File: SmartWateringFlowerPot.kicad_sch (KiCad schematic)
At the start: 0 parts

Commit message: Add first schematic draft
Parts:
- added C1: 10uF input, Capacitor_SMD:C_0805_2012Metric, symbol Device:C
- added C2: 22uF output, Capacitor_SMD:C_0805_2012Metric, symbol Device:C
- added C3: 100nF BST, Capacitor_SMD:C_0805_2012Metric, symbol Device:C
- added D1: SS34 flyback, Diode_SMD:D_SMA, symbol Device:D_Schottky
- added J1: USB-C 5V + USB2, symbol Connector:USB_C_Receptacle_USB2.0_14P
- added J2: PUMP 5V, Connector_JST:JST_XH_B2B-XH-A_1x02_P2.50mm_Vertical, symbol Connector_Generic:Conn_01x02
- added J3: MOISTURE, Connector_JST:JST_XH_B3B-XH-A_1x03_P2.50mm_Vertical, symbol Connector_Generic:Conn_01x03
- added J4: RESERVOIR_SW, Connector_JST:JST_XH_B2B-XH-A_1x02_P2.50mm_Vertical, symbol Connector_Generic:Conn_01x02
- added J5: FLOW optional, Connector_JST:JST_XH_B3B-XH-A_1x03_P2.50mm_Vertical, symbol Connector_Generic:Conn_01x03
- added J6: UI OLED/ENC/LED, Connector_JST:JST_XH_B9B-XH-A_1x09_P2.50mm_Vertical, symbol Connector_Generic:Conn_01x09
- added J7: DEBUG 3V3/GND/TX/RX/EN/BOOT, Connector_PinHeader_2.54mm:PinHeader_1x06_P2.54mm_Vertical, symbol Connector_Generic:Conn_01x06
- added L1: 2.2uH TBD, symbol Device:L
- added Q1: AO3400A, Package_TO_SOT_SMD:SOT-23, symbol Transistor_FET:Q_NMOS_GSD
- added R1: 5.1k CC1, Resistor_SMD:R_0805_2012Metric, symbol Device:R
- added R2: 5.1k CC2, Resistor_SMD:R_0805_2012Metric, symbol Device:R
- added R3: 10k EN pullup, Resistor_SMD:R_0805_2012Metric, symbol Device:R
- added R4: 220R gate, Resistor_SMD:R_0805_2012Metric, symbol Device:R
- added R5: 100k pulldown, Resistor_SMD:R_0805_2012Metric, symbol Device:R
- added R6: 4.7k SDA, Resistor_SMD:R_0805_2012Metric, symbol Device:R
- added R7: 4.7k SCL, Resistor_SMD:R_0805_2012Metric, symbol Device:R
- added R8: 10k reservoir pullup, Resistor_SMD:R_0805_2012Metric, symbol Device:R
- added U1: ESP32-S3-WROOM-1-N8, RF_Module:ESP32-S3-WROOM-1, symbol RF_Module:ESP32-S3-WROOM-1
- added U2: AP63203WU-7, Package_TO_SOT_SMD:TSOT-23-6, symbol Regulator_Switching:AP63200WU
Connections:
- new net: Q1.1 (G), R4.2, R5.1
- new net: D1.2 (A), J2.2 (Pin_2), Q1.3 (D)
- new net: J1.A5 (CC1), R1.1
- new net: J1.A6 (D+), J1.B6 (D+), U1.14 (USB_D+)
- new net: J1.A7 (D-), J1.B7 (D-), U1.13 (USB_D-)
- new net: J1.B5 (CC2), R2.1
- new net: R4.1, U1.4 (IO4)
- new net: J4.1 (Pin_1), R8.1, U1.21 (IO13)
- new net: C3.1, U2.6 (BST)
- new net: C3.2, L1.2, U2.5 (SW)
- new net: J6.4 (Pin_4), J6.7 (Pin_7), J7.4 (Pin_4), R7.2, U1.17 (IO9), U1.20 (IO12), U1.36 (RXD0)
- new net: J3.3 (Pin_3), U1.39 (IO1)
- new net: J5.3 (Pin_3), U1.22 (IO14)
- new net: J7.3 (Pin_3), J7.5 (Pin_5), R3.1, U1.3 (EN), U1.37 (TXD0)
- new net: J6.3 (Pin_3), J6.5 (Pin_5), J6.6 (Pin_6), J6.8 (Pin_8), J6.9 (Pin_9), R6.2, U1.12 (IO8), U1.18 (IO10), U1.19 (IO11), U1.8 (IO15), U1.9 (IO16)
- new net: J7.6 (Pin_6), U1.27 (IO0)
- new net +3V3: C2.1, J3.1 (Pin_1), J5.1 (Pin_1), J6.1 (Pin_1), J7.1 (Pin_1), L1.1, R3.2, R6.1, R7.1, R8.2, U1.2 (3V3), U2.1 (FB)
- new net +5V: C1.1, D1.1 (K), J1.A4 (VBUS), J1.A9 (VBUS), J1.B4 (VBUS), J1.B9 (VBUS), J2.1 (Pin_1), U2.2 (EN), U2.3 (IN)
- new net GND: C1.2, C2.2, J1.A1 (GND), J1.A12 (GND), J1.B1 (GND), J1.B12 (GND), J1.S1 (SHIELD), J3.2 (Pin_2), J4.2 (Pin_2), J5.2 (Pin_2), J6.2 (Pin_2), J7.2 (Pin_2), Q1.2 (S), R1.2, R2.2, R5.2, U1.1 (GND), U1.40 (GND), U1.41 (GND), U2.4 (GND)
- no-connect marks 0 -> 20
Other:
- note added: "3.3V buck regulator"
- note added: "AO3400A low-side driver: gate resistor, 100k pulldown, SS34 flyback diode."
- note added: "ESP32-S3 + connectors"
- note added: "FLOW_PULSE must be level shifted if selected sensor outputs 5V pulses."
- note added: "Follow AP63203 datasheet layout exactly: compact input cap, inductor, BST loop, and FB node."
- note added: "J6: 3V3, GND, SDA, SCL, ENC_A, ENC_B, ENC_SW, ERROR_LED, STATUS_LED."
- note added: "J7 pinout: 3V3, GND, TXD0, RXD0, EN, IO0/BOOT."
- note added: "MOISTURE_ADC uses IO1 / ADC1-capable pin. Sensor output must be <= 3.3V."
- note added: "Pump low-side driver"
- note added: "Reservoir switch default: pullup to 3V3, switch closes to GND."
- note added: "Smart Pot V2 Rev A - first schematic draft"
- note added: "USB D-/D+ routed to ESP32-S3 native USB pins."
- note added: "USB-C input + native USB"
- note added: "Verify exact footprints, connector pin order, ESP32 boot pins, and AP63203 layout before PCB routing."

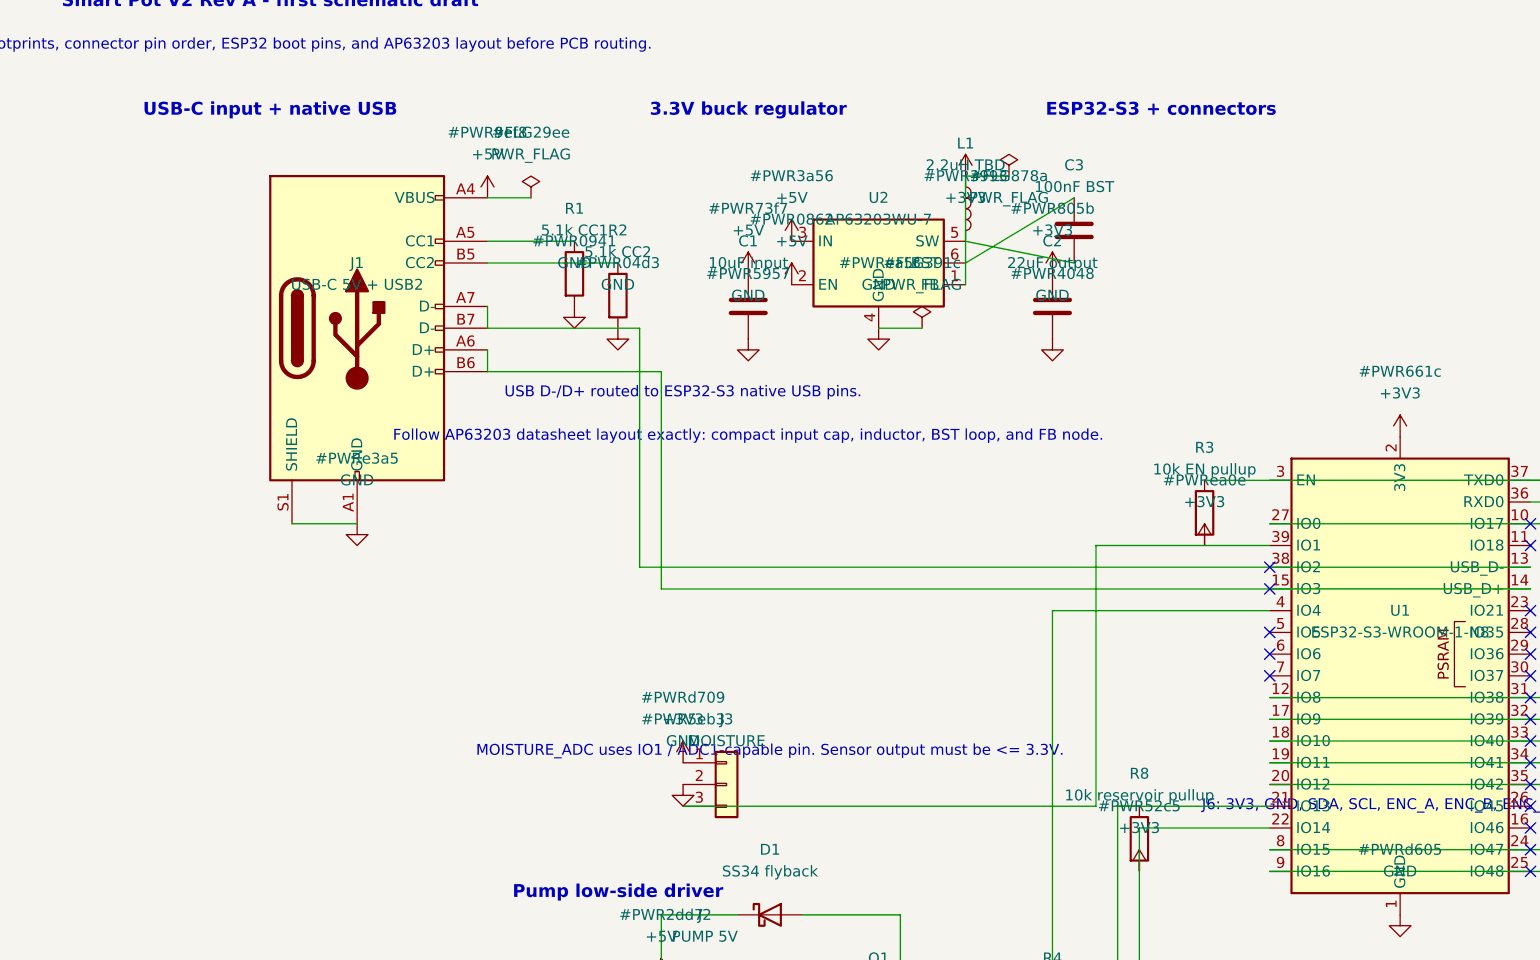
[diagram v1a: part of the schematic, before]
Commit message: Prepare schematic for PCB pass two
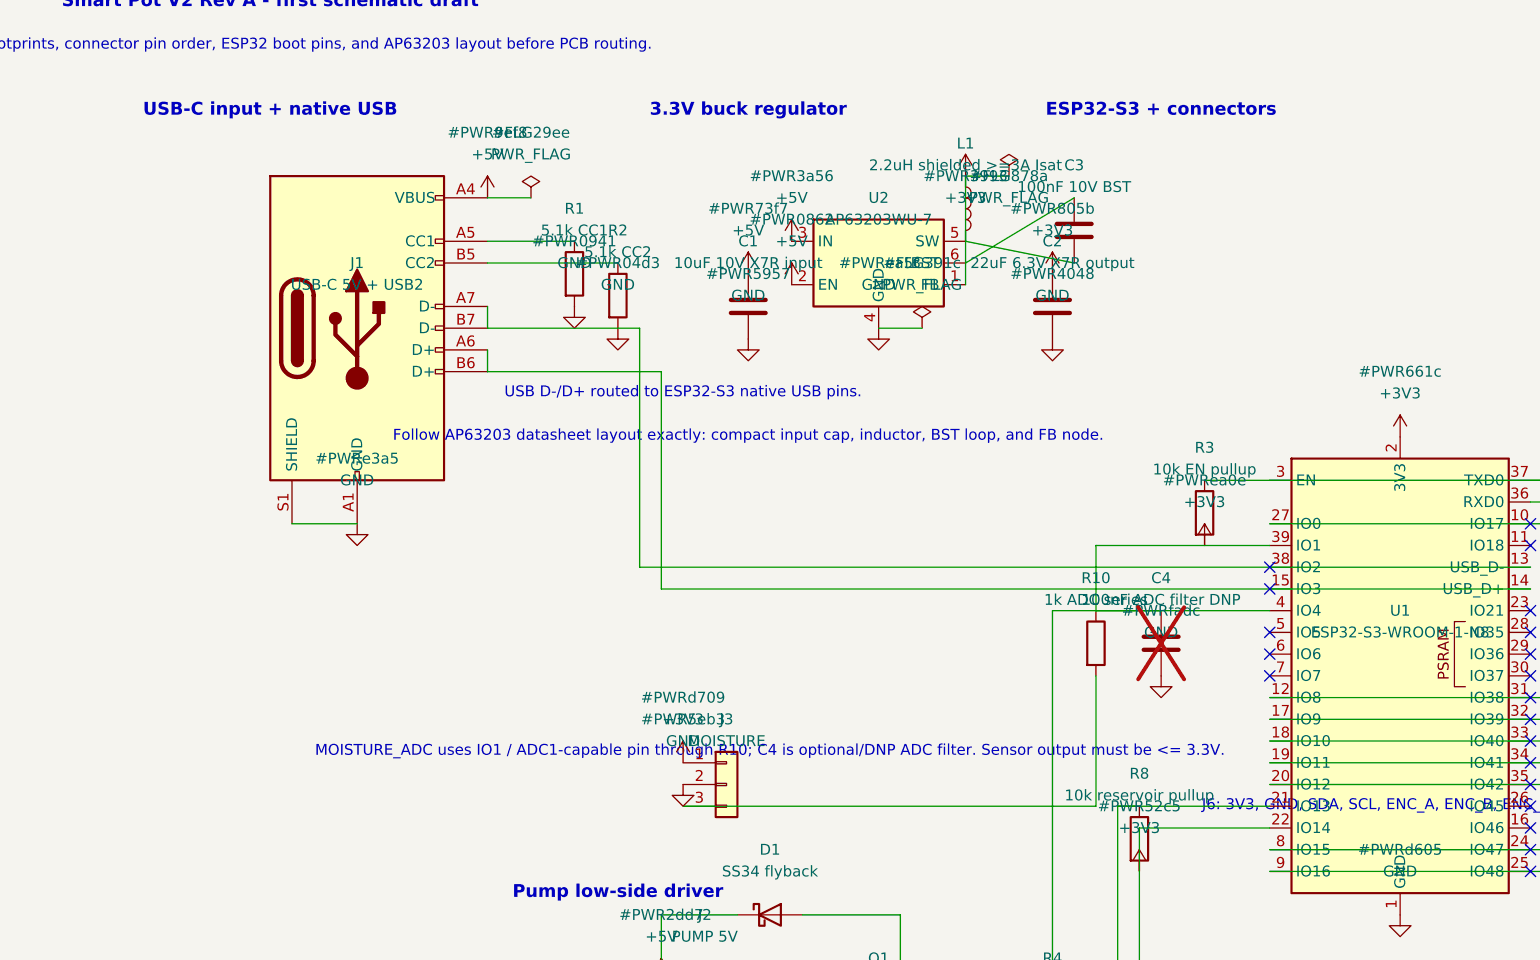
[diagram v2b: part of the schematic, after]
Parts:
- added C4: 100nF ADC filter DNP, Capacitor_SMD:C_0805_2012Metric, symbol Device:C
- added R10: 1k ADC series, Resistor_SMD:R_0805_2012Metric, symbol Device:R
- C1: value 10uF input -> 10uF 10V X7R input
- C2: value 22uF output -> 22uF 6.3V X7R output
- C3: value 100nF BST -> 100nF 10V BST
- J1: footprint (none) -> Connector_USB:USB_C_Receptacle_GCT_USB4105-xx-A_16P_TopMnt_Horizontal
- L1: value 2.2uH TBD -> 2.2uH shielded >=3A Isat; footprint (none) -> Inductor_SMD:L_Bourns_SRN6045TA
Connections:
- net GND: now also C4.2
- net at R4.1, U1.4 (IO4): now also U1.39 (IO1), C4.1, R10.1
- net at J3.3 (Pin_3): now also R10.2; no longer U1.39 (IO1)
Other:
- note added: "MOISTURE_ADC uses IO1 / ADC1-capable pin through R10; C4 is optional/DNP ADC filter. Sensor output must be <= 3.3V."
- note removed: "MOISTURE_ADC uses IO1 / ADC1-capable pin. Sensor output must be <= 3.3V."
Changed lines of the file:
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@@
 			)
 		)
-		(property "Footprint" ""
+		(property "Footprint" "Connector_USB:USB_C_Receptacle_GCT_USB4105-xx-A_16P_TopMnt_Horizontal"
 			(at 30.48 55.879999999999995 0)
 			(effects (font (size 1.27 1.27)) (hide yes))
@@
 			)
 		)
-		(property "Value" "2.2uH TBD"
+		(property "Value" "2.2uH shielded >=3A Isat"
 			(at 101.6 31.75 0)
 			(effects
@@
 			)
 		)
-		(property "Footprint" ""
+		(property "Footprint" "Inductor_SMD:L_Bourns_SRN6045TA"
 			(at 101.6 41.91 0)
 			(effects (font (size 1.27 1.27)) (hide yes))
 		)
-		(property "Datasheet" "~"
+		(property "Datasheet" "https://www.bourns.com/docs/product-datasheets/srn6045ta.pdf"
 			(at 101.6 44.449999999999996 0)
 			(effects (font (size 1.27 1.27)) (hide yes))
@@
 			)
 		)
-		(property "Value" "10uF input"
+		(property "Value" "10uF 10V X7R input"
 			(at 76.2 43.18 0)
 			(effects
@@
 			)
 		)
-		(property "Value" "22uF output"
+		(property "Value" "22uF 6.3V X7R output"
 			(at 111.76 43.18 0)
 			(effects
@@
 			)
 		)
-		(property "Value" "100nF BST"
+		(property "Value" "100nF 10V BST"
 			(at 114.3 34.29 0)
 			(effects
@@
 	(wire
 		(pts
-			(xy 116.84 106.68) (xy 116.84 76.20)
-		)
-		(stroke
-			(width 0)
-			(type default)
+			(xy 116.84 106.68) (xy 116.84 91.44)
+		)
+		(stroke
+			(width 0)
+			(type default)
+		)
+	)
+	(wire
+		(pts
+			(xy 116.84 83.82) (xy 116.84 76.20)
+		)
+		(stroke
+			(width 0)
+			(type default)
+		)
+	)
+	(symbol
+		(lib_id "Device:R")
+		(at 116.84 87.63 0)
+		(unit 1)
+		(exclude_from_sim no)
+		(in_bom yes)
+		(on_board yes)
+		(dnp no)
+		(property "Reference" "R10"
+			(at 116.84 80.01 0)
+			(effects
+				(font
+					(size 1.27 1.27)
+				)
+			)
+		)
+		(property "Value" "1k ADC series"
+			(at 116.84 82.55 0)
+			(effects
+				(font
+					(size 1.27 1.27)
+				)
+			)
+		)
+		(property "Footprint" "Resistor_SMD:R_0805_2012Metric"
+			(at 116.84 92.71 0)
+			(effects (font (size 1.27 1.27)) (hide yes))
+		)
+		(property "Datasheet" "~"
+			(at 116.84 95.25 0)
+			(effects (font (size 1.27 1.27)) (hide yes))
+		)
+		(pin "1"
+		)
+		(pin "2"
+		)
+		(instances
+			(project ""
+				(path "/f5104368-02d7-408f-bed6-2d0faa538216"
+					(reference "R10")
+					(unit 1)
+				)
+			)
+		)
+	)
+	(symbol
+		(lib_id "Device:C")
+		(at 124.46 87.63 0)
+		(unit 1)
+		(exclude_from_sim no)
+		(in_bom yes)
+		(on_board yes)
+		(dnp yes)
+		(property "Reference" "C4"
+			(at 124.46 80.01 0)
+			(effects
+				(font
+					(size 1.27 1.27)
+				)
+			)
+		)
+		(property "Value" "100nF ADC filter DNP"
+			(at 124.46 82.55 0)
+			(effects
+				(font
+					(size 1.27 1.27)
+				)
+			)
+		)
+		(property "Footprint" "Capacitor_SMD:C_0805_2012Metric"
+			(at 124.46 92.71 0)
+			(effects (font (size 1.27 1.27)) (hide yes))
+		)
+		(property "Datasheet" "~"
+			(at 124.46 95.25 0)
+			(effects (font (size 1.27 1.27)) (hide yes))
+		)
+		(pin "1"
+		)
+		(pin "2"
+		)
+		(instances
+			(project ""
+				(path "/f5104368-02d7-408f-bed6-2d0faa538216"
+					(reference "C4")
+					(unit 1)
+				)
+			)
+		)
+	)
+	(wire
+		(pts
+			(xy 116.84 83.82) (xy 124.46 83.82)
+		)
+		(stroke
+			(width 0)
+			(type default)
+		)
+	)
+	(symbol
+		(lib_id "power:GND")
+		(at 124.46 91.44 0)
+		(unit 1)
+		(exclude_from_sim no)
+		(in_bom no)
+		(on_board no)
+		(dnp no)
+		(property "Reference" "#PWRfadc"
+			(at 124.46 83.82 0)
+			(effects
+				(font
+					(size 1.27 1.27)
+				)
+			)
+		)
+		(property "Value" "GND"
+			(at 124.46 86.36 0)
+			(effects
+				(font
+					(size 1.27 1.27)
+				)
+			)
+		)
+		(property "Footprint" "Connector_USB:USB_C_Receptacle_GCT_USB4105-xx-A_16P_TopMnt_Horizontal"
+			(at 124.46 96.52 0)
+			(effects (font (size 1.27 1.27)) (hide yes))
+		)
+		(property "Datasheet" "~"
+			(at 124.46 99.06 0)
+			(effects (font (size 1.27 1.27)) (hide yes))
+		)
+		(pin "1"
+		)
+		(instances
+			(project ""
+				(path "/f5104368-02d7-408f-bed6-2d0faa538216"
+					(reference "#PWRfadc")
+					(unit 1)
+				)
+			)
 		)
 	)
@@
 		)
 	)
-	(text "MOISTURE_ADC uses IO1 / ADC1-capable pin. Sensor output must be <= 3.3V."
+	(text "MOISTURE_ADC uses IO1 / ADC1-capable pin through R10; C4 is optional/DNP ADC filter. Sensor output must be <= 3.3V."
 		(at 78.74 100.33 0)
 		(effects

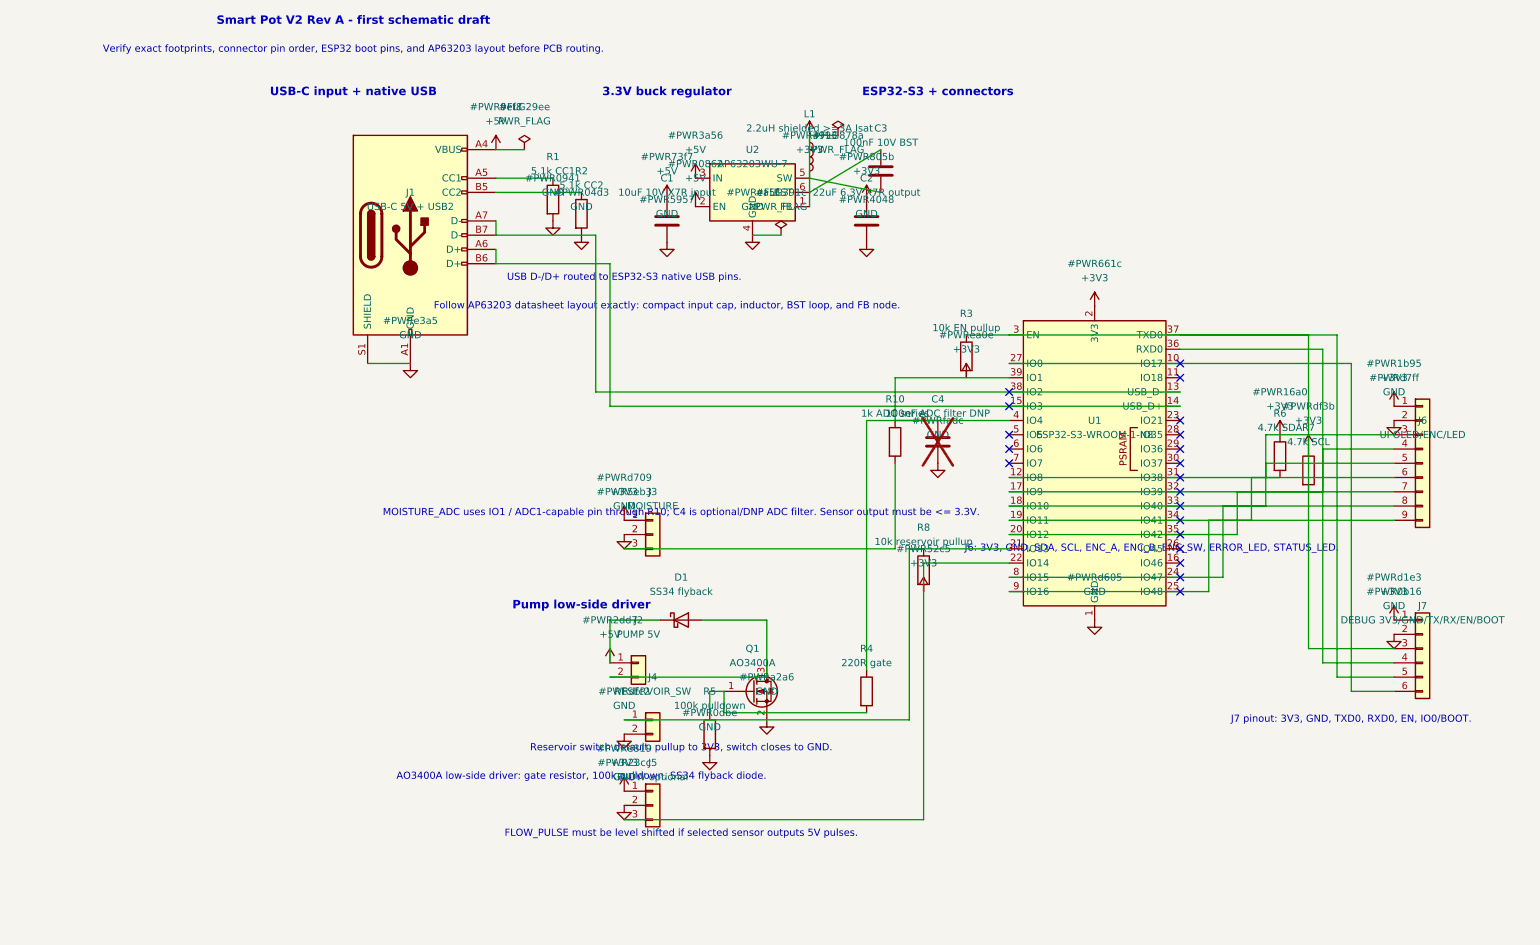
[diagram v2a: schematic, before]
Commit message: Improve schematic reliability for PCB readiness
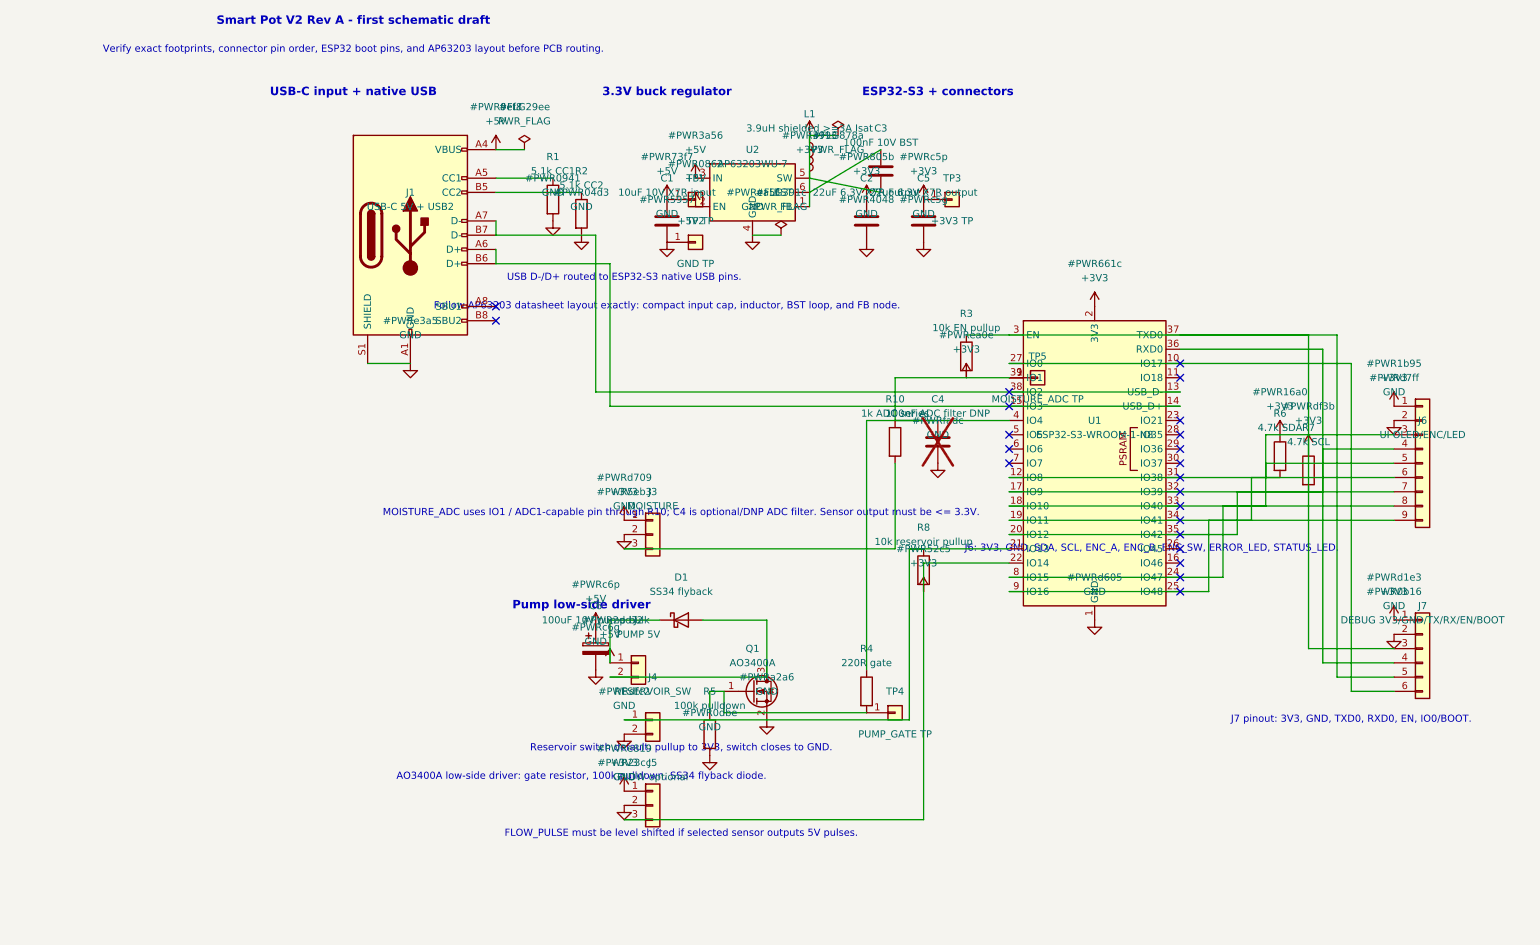
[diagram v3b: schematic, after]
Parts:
- added C5: 22uF 6.3V X7R output, Capacitor_SMD:C_0805_2012Metric, symbol Device:C
- added C6: 100uF 10V pump bulk, Capacitor_THT:CP_Radial_D6.3mm_P2.50mm, symbol Device:C_Polarized
- added TP1: +5V TP, TestPoint:TestPoint_Pad_D1.5mm, symbol Connector_Generic:Conn_01x01
- added TP2: GND TP, TestPoint:TestPoint_Pad_D1.5mm, symbol Connector_Generic:Conn_01x01
- added TP3: +3V3 TP, TestPoint:TestPoint_Pad_D1.5mm, symbol Connector_Generic:Conn_01x01
- added TP4: PUMP_GATE TP, TestPoint:TestPoint_Pad_D1.5mm, symbol Connector_Generic:Conn_01x01
- added TP5: MOISTURE_ADC TP, TestPoint:TestPoint_Pad_D1.5mm, symbol Connector_Generic:Conn_01x01
- J1: symbol Connector:USB_C_Receptacle_USB2.0_14P -> Connector:USB_C_Receptacle_USB2.0_16P
- L1: value 2.2uH shielded >=3A Isat -> 3.9uH shielded >=3A Isat
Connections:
- net +3V3: now also C5.1, TP3.1 (Pin_1)
- net +5V: now also C6.1, TP1.1 (Pin_1)
- net GND: now also C5.2, C6.2, TP2.1 (Pin_1)
- net at Q1.1 (G), R4.2, R5.1: now also TP4.1 (Pin_1)
- net at C4.1, R10.1, R4.1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: now also TP5.1 (Pin_1)
- no-connect marks 20 -> 22
